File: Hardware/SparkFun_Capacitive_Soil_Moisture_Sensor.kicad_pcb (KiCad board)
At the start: 2 copper layers, 15.3 x 57.1 mm, 24 parts, among them J1 Qwiic_RA, J2 Qwiic_RA, U1 CAP1203

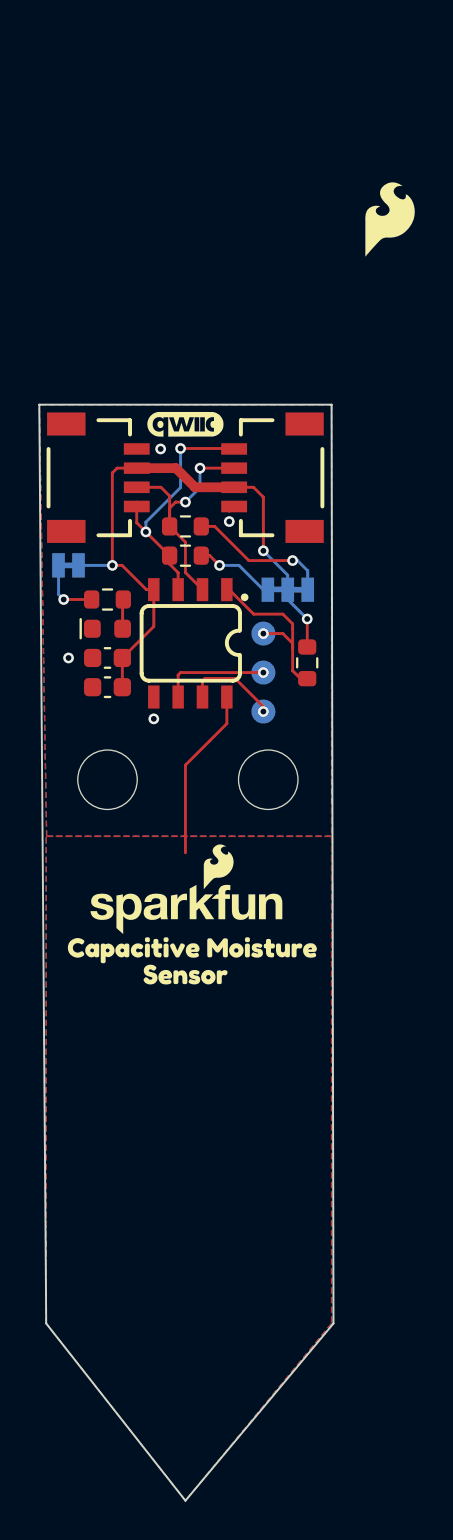
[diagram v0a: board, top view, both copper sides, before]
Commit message: Cleanup test points and silkscreen, remove acid traps
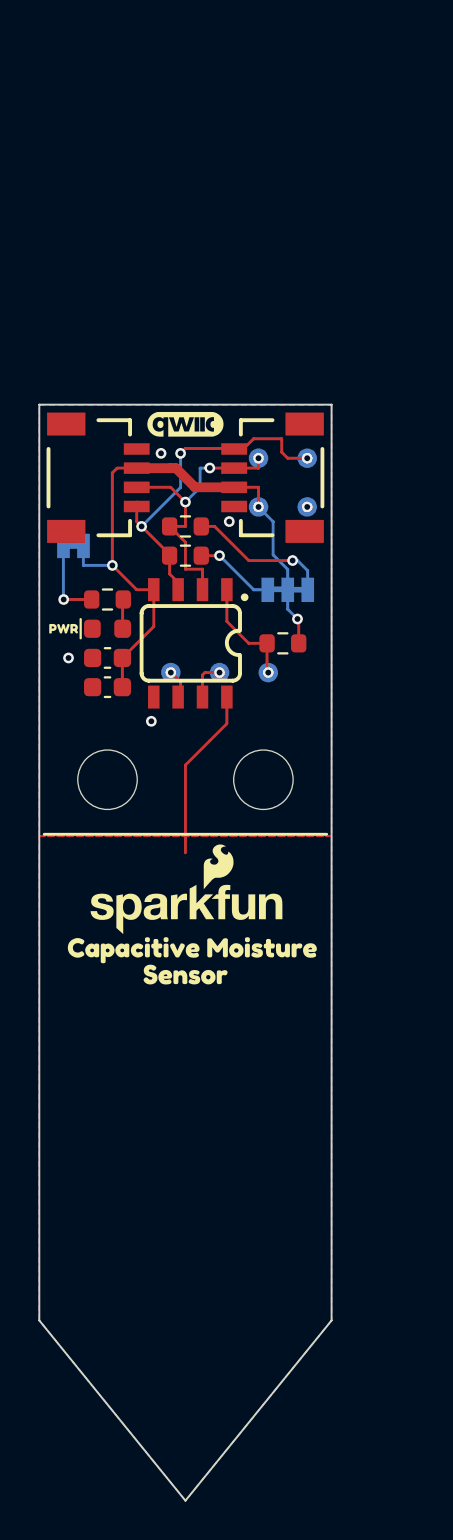
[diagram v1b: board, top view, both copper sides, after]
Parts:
- added TP4: 1.0mm, SparkFun-Connector:TestPoint-1.0mm, B.Cu at (121.9, 72.6)
- added TP5: 1.0mm, SparkFun-Connector:TestPoint-1.0mm, B.Cu at (119.4, 72.6)
- added TP6: 1.0mm, SparkFun-Connector:TestPoint-1.0mm, B.Cu at (119.4, 70.1)
- added TP7: 1.0mm, SparkFun-Connector:TestPoint-1.0mm, B.Cu at (121.9, 70.1)
- added kibuzzard-67ED66FD: G***, kibuzzard-67ED66FD, B.Cu at (115.9, 97.0)
- added kibuzzard-6930CD50: G***, kibuzzard-6930CD50, B.Cu at (115.6, 95.8)
- added kibuzzard-69334C1A: G***, kibuzzard-69334C1A, B.Cu at (112.5, 74.7)
- added kibuzzard-69334F28: G***, kibuzzard-69334F28, F.Cu at (109.2, 79.0)
- added kibuzzard-693350BE: G***, kibuzzard-693350BE, B.Cu at (117.9, 77.0)
- added kibuzzard-69371667: G***, kibuzzard-69371667, B.Cu at (119.4, 69.1)
- added kibuzzard-6937166E: G***, kibuzzard-6937166E, B.Cu at (121.9, 69.1)
- added kibuzzard-69371675: G***, kibuzzard-69371675, B.Cu at (119.4, 71.6)
- added kibuzzard-6937167A: G***, kibuzzard-6937167A, B.Cu at (121.9, 71.6)
- added kibuzzard-69371C9D: G***, kibuzzard-69371C9D, B.Cu at (114.8, 80.3)
- added kibuzzard-69371CAB: G***, kibuzzard-69371CAB, B.Cu at (117.3, 80.3)
- added kibuzzard-69373B6F: G***, kibuzzard-69373B6F, B.Cu at (119.9, 80.3)
- G***: moved to B.Cu
- TP1, TP2, TP3: value 1.25mm -> 1.0mm; footprint SparkFun-Connector:TestPoint-1.25mm -> SparkFun-Connector:TestPoint-1.0mm
- moved G*** 35.6 mm to (115.9, 93.5)
- moved G*** 20.4 mm to (110.2, 70.4), turned to 180 degrees
- moved TP3 5.24 mm to (114.8, 81.3)
- moved TP2 2.29 mm to (117.3, 81.3)
- moved TP1 2.05 mm to (119.9, 81.3)
- moved R2 1.63 mm to (120.7, 79.8), turned to 180 degrees
- moved JP1 1.05 mm to (109.7, 74.7)
- moved ST2 0.25 mm to (119.6, 86.9)
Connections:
- TP2 pad 1: Net-(U1-CS3) -> Net-(U1-CS2)
- TP3 pad 1: Net-(U1-CS2) -> Net-(U1-CS3)
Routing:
- net SCL: track 13.4 -> 17.9 mm, vias 2 -> 3
- net Net-(U1-CS3): track 5.65 -> 1.54 mm
- net ~{ALERT}: track 9.53 -> 5.90 mm
- net Net-(U1-CS2): track 4.93 -> 1.84 mm
- net SDA: track 13.3 -> 15.1 mm, vias 2 -> 3
- net Net-(JP1-A): track 3.35 -> 4.26 mm
- net 3.3V: track 32.4 -> 32.9 mm
- net GND: track 0.41 -> 0.02 mm, vias 4 -> 5
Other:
- board size 15.3 x 57.1 mm -> 15.2 x 57.1 mm

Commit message: Add functional changes to PCB from review.
Achieves MVP, does not have all requested aesthetic changes.
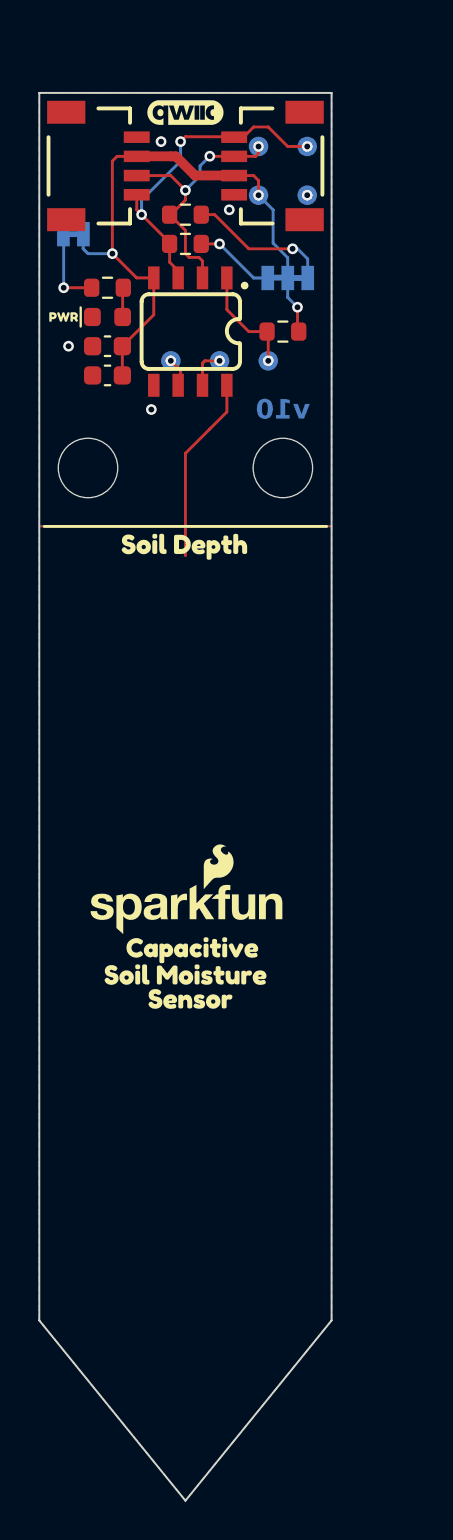
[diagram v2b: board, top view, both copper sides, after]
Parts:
- removed the kibuzzard-67ED66FD at (115.6, 97.0)
- removed the kibuzzard-67ED66FD at (115.9, 97.0)
- removed kibuzzard-6930CD50 (x2): G***, kibuzzard-6930CD50
- added kibuzzard-67ED66FD: G***, kibuzzard-67ED66FD, F.Cu at (115.8, 98.3)
- added kibuzzard-67ED66FD: G***, kibuzzard-67ED66FD, B.Cu at (115.6, 98.3)
- added kibuzzard-6938A9B9: G***, kibuzzard-6938A9B9, F.Cu at (115.9, 95.8)
- added kibuzzard-6938A9B9: G***, kibuzzard-6938A9B9, B.Cu at (115.5, 95.8)
- added kibuzzard-6938A9C3: G***, kibuzzard-6938A9C3, F.Cu at (115.6, 97.0)
- added kibuzzard-6938A9C3: G***, kibuzzard-6938A9C3, B.Cu at (115.8, 97.0)
- added kibuzzard-6938B677: G***, kibuzzard-6938B677, F.Cu at (115.5, 74.7)
- added kibuzzard-6938B677: G***, kibuzzard-6938B677, B.Cu at (115.5, 74.7)
- moved ST2 16.3 mm to (120.7, 70.6)
- moved ST4 16.3 mm to (110.5, 70.6)
- moved G*** 16.3 mm to (110.2, 54.1)
- moved J1 16.3 mm to (113.0, 54.9)
- moved J2 16.3 mm to (118.1, 54.9)
- moved TP4 16.3 mm to (121.9, 56.4)
- moved TP5 16.3 mm to (119.4, 56.4)
- moved C1 16.3 mm to (111.5, 65.8)
- moved C2 16.3 mm to (111.5, 64.3)
- moved D1 16.3 mm to (111.5, 62.7)
- moved JP1 16.3 mm to (109.7, 58.4)
- moved JP4 16.3 mm to (120.9, 60.7)
- moved R1 16.3 mm to (111.5, 61.2)
- moved R2 16.3 mm to (120.7, 63.5)
- moved R3 16.3 mm to (115.6, 58.9)
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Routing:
- net SDA: track 15.1 -> 14.1 mm
- net TO_CAP_PLATE: track 9.02 -> 9.78 mm
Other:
- board size 15.2 x 57.1 mm -> 15.2 x 73.4 mm
- board text added: "Finish: Lead-Free HASL"
- board text added: "Layers: 2"
- board text added: "v10"
- board text removed: "Controlled Impedance: JLC04161H-7628"
- board text removed: "Finish: ENIG"
- board text removed: "Inner Copper Weight: 0.5oz"
- board text removed: "Layers: 4"
- board text removed: "No Clean Process"

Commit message: Add ruler to silkscreen on PCB
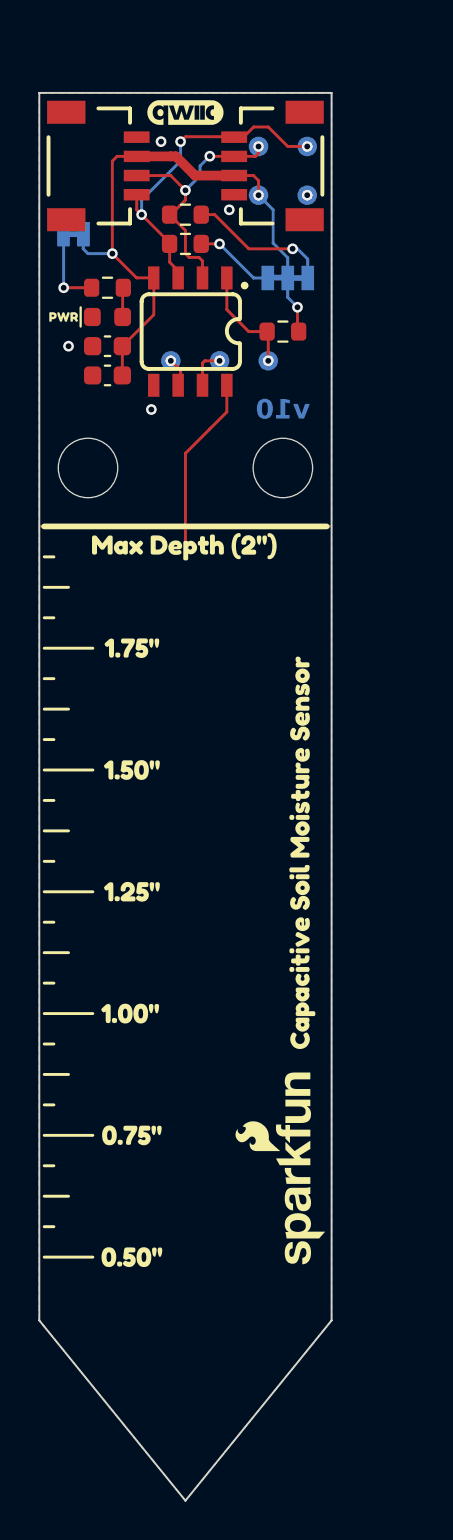
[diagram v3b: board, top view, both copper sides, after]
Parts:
- removed kibuzzard-67ED66FD (x2): G***, kibuzzard-67ED66FD
- removed kibuzzard-6938A9B9 (x2): G***, kibuzzard-6938A9B9
- removed kibuzzard-6938A9C3 (x2): G***, kibuzzard-6938A9C3
- removed kibuzzard-6938B677 (x2): G***, kibuzzard-6938B677
- added kibuzzard-693B4BBA: G***, kibuzzard-693B4BBA, F.Cu at (112.8, 111.8)
- added kibuzzard-693B4BBA: G***, kibuzzard-693B4BBA, B.Cu at (118.4, 111.8)
- added kibuzzard-693B4BC8: G***, kibuzzard-693B4BC8, F.Cu at (112.8, 105.4)
- added kibuzzard-693B4BC8: G***, kibuzzard-693B4BC8, B.Cu at (118.4, 105.4)
- added kibuzzard-693B4BFF: G***, kibuzzard-693B4BFF, F.Cu at (112.7, 99.1)
- added kibuzzard-693B4BFF: G***, kibuzzard-693B4BFF, B.Cu at (118.5, 99.1)
- added kibuzzard-693B4C16: G***, kibuzzard-693B4C16, F.Cu at (112.8, 92.7)
- added kibuzzard-693B4C16: G***, kibuzzard-693B4C16, B.Cu at (118.4, 92.7)
- added kibuzzard-693B4C27: G***, kibuzzard-693B4C27, F.Cu at (112.8, 86.4)
- added kibuzzard-693B4C27: G***, kibuzzard-693B4C27, B.Cu at (118.4, 86.4)
- added kibuzzard-693B4C3E: G***, kibuzzard-693B4C3E, F.Cu at (112.8, 80.0)
- added kibuzzard-693B4C3E: G***, kibuzzard-693B4C3E, B.Cu at (118.4, 80.0)
- added kibuzzard-693B4C4C: G***, kibuzzard-693B4C4C, F.Cu at (115.5, 74.7)
- added kibuzzard-693B4C5A: G***, kibuzzard-693B4C5A, B.Cu at (115.5, 74.7)
- added kibuzzard-693B565E: G***, kibuzzard-693B565E, F.Cu at (121.7, 90.7)
- added kibuzzard-693B565E: G***, kibuzzard-693B565E, B.Cu at (109.5, 90.7)
- moved G*** 15.0 mm to (109.7, 107.2), turned to 90 degrees
- moved G*** 14.9 mm to (121.4, 107.2), turned to 90 degrees

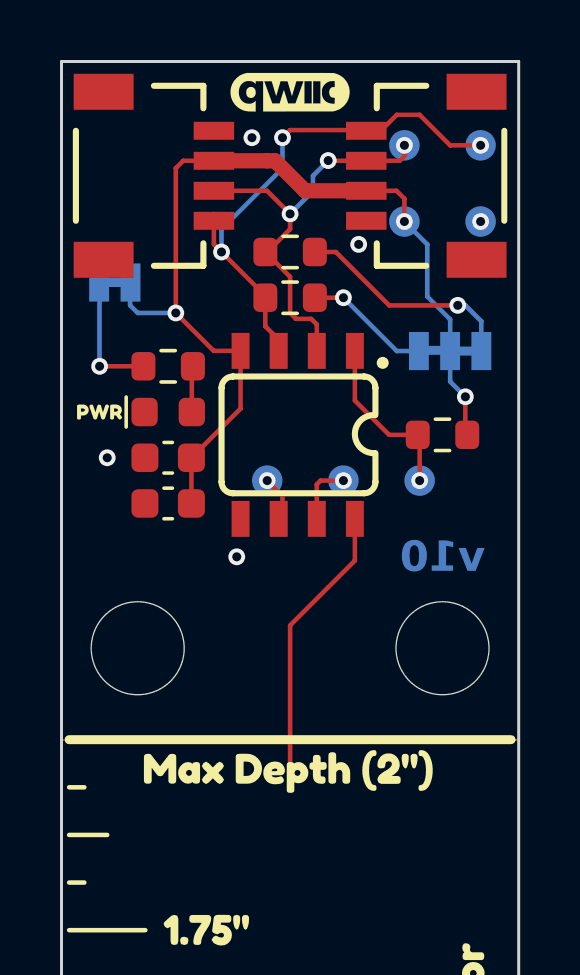
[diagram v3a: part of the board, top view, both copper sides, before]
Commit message: Update PCB with new CY8CMBR3 IC
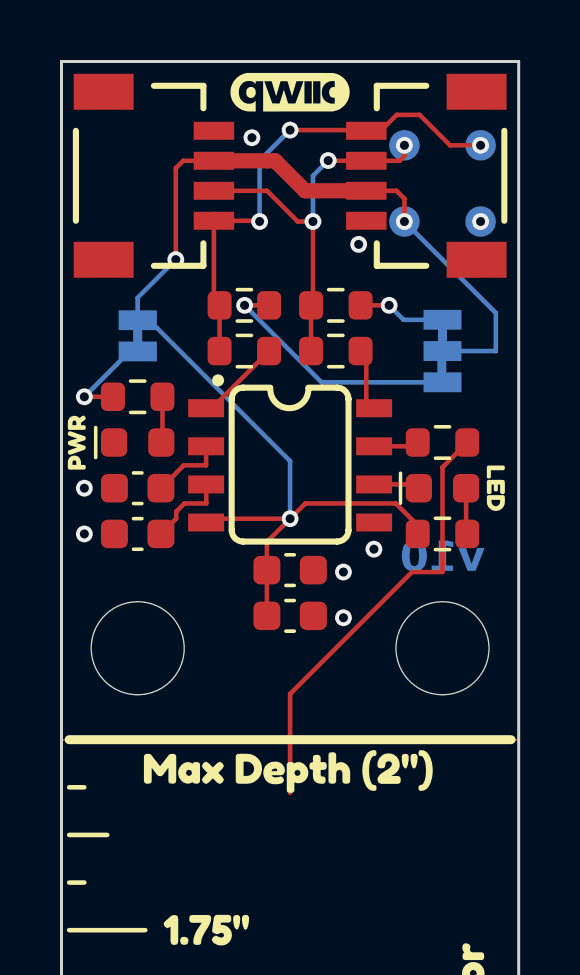
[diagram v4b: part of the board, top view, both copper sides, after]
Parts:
- removed the G*** at (110.2, 54.1)
- removed the R2 at (120.7, 63.5)
- removed TP1, TP2, TP3: 1.0mm, SparkFun-Connector:TestPoint-1.0mm
- removed kibuzzard-69334F28: G***, kibuzzard-69334F28
- removed kibuzzard-69371C9D: G***, kibuzzard-69371C9D
- removed kibuzzard-69371CAB: G***, kibuzzard-69371CAB
- removed kibuzzard-69373B6F: G***, kibuzzard-69373B6F
- added C3: 2200pF, SparkFun-Capacitor:C_0603_1608Metric, F.Cu at (110.5, 65.3)
- added C4: 0.1uF, SparkFun-Capacitor:C_0603_1608Metric, F.Cu at (110.5, 66.8)
- added D2: Red, SparkFun-LED:LED_0603_1608Metric_Red, F.Cu at (120.7, 65.3)
- added R4: 330, SparkFun-Resistor:R_0603_1608Metric, F.Cu at (117.1, 60.7)
- added R5: 330, SparkFun-Resistor:R_0603_1608Metric, F.Cu at (114.0, 60.7)
- added R6: 560, SparkFun-Resistor:R_0603_1608Metric, F.Cu at (120.7, 63.8)
- added R7: 4.7k, SparkFun-Resistor:R_0603_1608Metric, F.Cu at (120.7, 66.8)
- added Ref**: Val**, SparkFun-Aesthetic:OSHW_Logo_2.5mm, B.Cu at (110.2, 54.6)
- added kibuzzard-693C8DDA: G***, kibuzzard-693C8DDA, F.Cu at (108.5, 63.8)
- added kibuzzard-693C8DE4: G***, kibuzzard-693C8DE4, F.Cu at (122.4, 65.3)
- U1: value CAP1203 -> CY8CMBR3102
- moved C1 5.53 mm to (115.6, 69.5), turned to 0 degrees
- moved C2 5.53 mm to (115.6, 68.0), turned to 0 degrees
- moved R3 2.34 mm to (117.1, 59.2)
- moved JP1 1.93 mm to (110.5, 60.2), turned to 90 degrees
- moved kibuzzard-69334C1A 1.85 mm to (113.0, 60.2)
- moved R2 1.55 mm to (114.0, 59.2)
- moved D1 1.44 mm to (110.5, 63.8)
- moved R1 1.44 mm to (110.5, 62.2)
- moved U1 1.05 mm to (115.6, 64.5), turned to 0 degrees
- moved kibuzzard-693350BE 0.51 mm to (118.4, 60.7)
- moved JP2 0.25 mm to (120.7, 60.7), turned to -90 degrees
- renumbered JP4 to JP2, R3 to R2, R5 to R3
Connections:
- U1 pad 1: ~{ALERT} -> Net-(U1-SCL)
- U1 pad 2: SDA -> Net-(U1-CMOD)
- U1 pad 3: SCL -> Net-(U1-VCC)
- U1 pad 8: TO_CAP_PLATE -> Net-(U1-SDA)
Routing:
- net 3.3V: track 32.7 -> 42.4 mm
- net ~{ALERT}: track 5.90 -> 0.00 mm, vias 1 -> 0
- net TO_CAP_PLATE: track 9.78 -> 14.7 mm
- net Net-(JP2-A): track 7.50 -> 2.93 mm
- net Net-(JP2-C): track 4.20 -> 8.48 mm
- net Net-(U1-SCL): track 0.00 -> 2.89 mm
- net Net-(U1-VCC): track 0.00 -> 2.71 mm
- net Net-(U1-CMOD): track 0.00 -> 2.46 mm
- net Net-(U1-SDA): track 0.00 -> 2.09 mm
- net Net-(D2-A): track 0.00 -> 1.54 mm
- net Net-(JP1-A): track 4.26 -> 3.36 mm
- net SCL: track 17.5 -> 16.7 mm
- net SDA: track 14.1 -> 13.3 mm
- net Net-(U1-CS0): track 1.84 -> 1.51 mm, vias 1 -> 0
- net GND: track 0.02 -> 0.00 mm, vias 5 -> 8
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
